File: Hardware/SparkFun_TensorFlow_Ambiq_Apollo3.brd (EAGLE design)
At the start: 40 x 40 mm, 95 parts, among them J5 CORTEX_DEBUG, J7 CAMERA-HIMAX, U2 LIS2DH12, U3 1.8V, U5 ARTEMIS_MODULESMD, Y2 32.768kHz

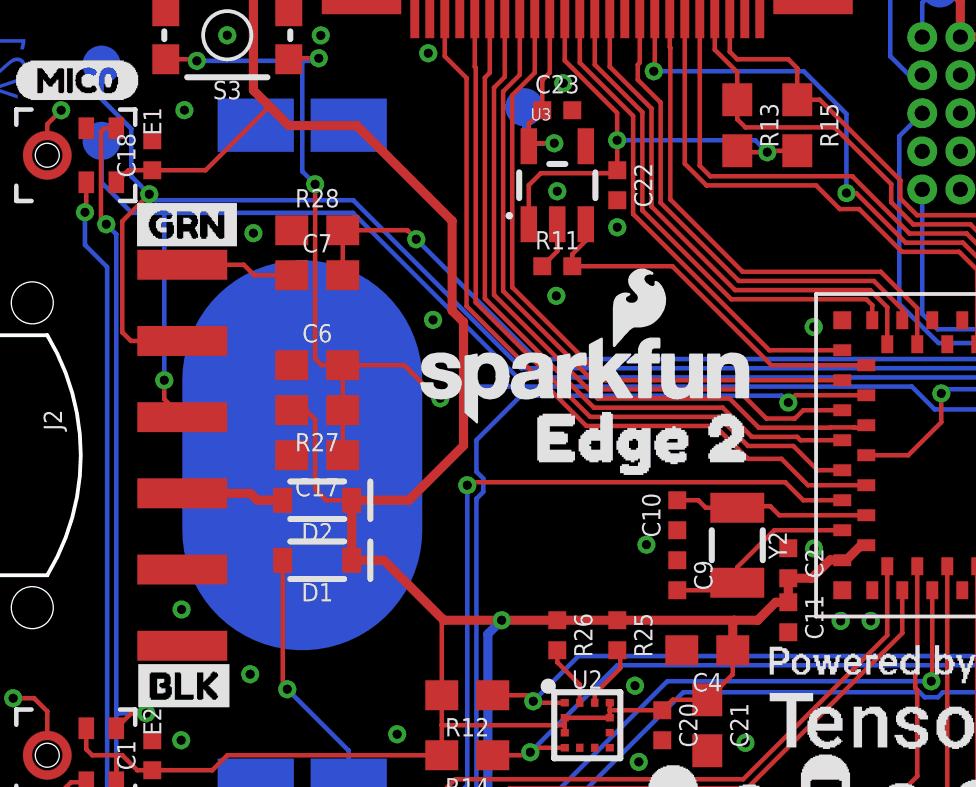
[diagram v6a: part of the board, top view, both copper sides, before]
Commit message: Move parts to fill gap left by DNP resistor removal. Change text in sch from Apollo3 to Artemis.
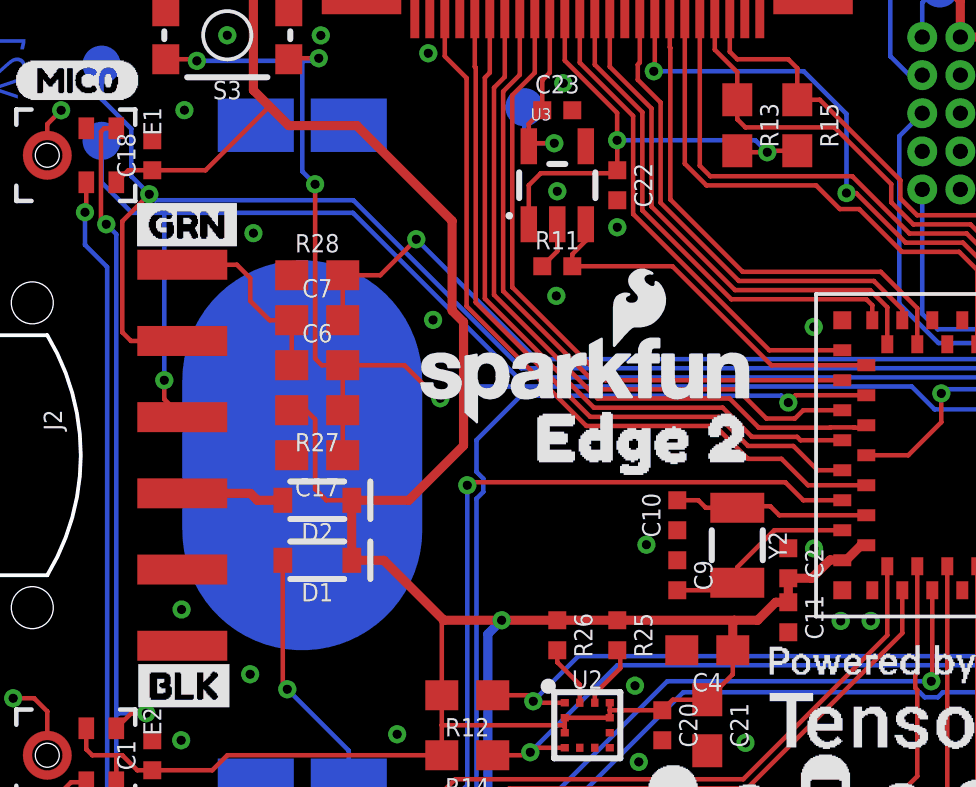
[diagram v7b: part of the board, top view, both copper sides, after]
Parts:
- moved C7 1.50 mm to (11.0, 24.5)
- moved R28 1.50 mm to (11.0, 26.0)
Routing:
- net !DTR: track 3.79 -> 6.36 mm
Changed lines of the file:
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@@
 <attribute name="VALUE" x="11" y="22.238" size="0.6096" layer="27" font="vector" ratio="20" align="top-center"/>
 </element>
-<element name="R28" library="SparkFun-Resistors" package="0603" value="220k" x="11" y="27.5" smashed="yes">
-<attribute name="NAME" x="11" y="28.262" size="0.6096" layer="25" font="vector" ratio="20" align="bottom-center"/>
-<attribute name="PROD_ID" value="RES-08969" x="11" y="23.69" size="1.778" layer="27" font="vector" ratio="15" display="off"/>
-<attribute name="VALUE" value="220k" x="11" y="26.738" size="0.6096" layer="27" font="vector" ratio="20" align="top-center"/>
-</element>
-<element name="C7" library="SparkFun-Capacitors" package="0603" value="0.1uF" x="11" y="26" smashed="yes">
+<element name="R28" library="SparkFun-Resistors" package="0603" value="220k" x="11" y="26" smashed="yes">
 <attribute name="NAME" x="11" y="26.762" size="0.6096" layer="25" font="vector" ratio="20" align="bottom-center"/>
-<attribute name="PROD_ID" value="CAP-00810" x="11" y="14.57" size="1.778" layer="27" font="vector" ratio="15" display="off"/>
-<attribute name="VALUE" value="0.1uF" x="11" y="25.238" size="0.6096" layer="27" font="vector" ratio="20" align="top-center"/>
+<attribute name="PROD_ID" value="RES-08969" x="11" y="22.19" size="1.778" layer="27" font="vector" ratio="15" display="off"/>
+<attribute name="VALUE" value="220k" x="11" y="25.238" size="0.6096" layer="27" font="vector" ratio="20" align="top-center"/>
+</element>
+<element name="C7" library="SparkFun-Capacitors" package="0603" value="0.1uF" x="11" y="24.5" smashed="yes">
+<attribute name="NAME" x="11" y="25.262" size="0.6096" layer="25" font="vector" ratio="20" align="bottom-center"/>
+<attribute name="PROD_ID" value="CAP-00810" x="11" y="13.07" size="1.778" layer="27" font="vector" ratio="15" display="off"/>
+<attribute name="VALUE" value="0.1uF" x="11" y="23.738" size="0.6096" layer="27" font="vector" ratio="20" align="top-center"/>
 </element>
 <element name="C17" library="SparkFun-Capacitors" package="0603" value="1nF" x="11" y="20" smashed="yes" rot="R180">
@@
 <wire x1="16.6858" y1="14.0408" x2="17.145" y2="14.5" width="0.3048" layer="16"/>
 <wire x1="26.7" y1="15.9" x2="26.7" y2="15.1" width="0.3048" layer="1"/>
-<wire x1="26.796" y1="15.1" x2="26.7" y2="15.1" width="0.3048" layer="1"/>
 <wire x1="24.9" y1="14.5" x2="25.68105" y2="14.5" width="0.3048" layer="1"/>
 <wire x1="26.28105" y1="15.1" x2="26.7" y2="15.1" width="0.3048" layer="1"/>
@@
 <contactref element="C7" pad="1"/>
 <contactref element="C6" pad="1"/>
-<wire x1="6.5" y1="26.35" x2="8.55" y2="26.35" width="0.1524" layer="1"/>
-<wire x1="8.55" y1="26.35" x2="8.9" y2="26" width="0.1524" layer="1"/>
-<wire x1="8.9" y1="26" x2="10.15" y2="26" width="0.1524" layer="1"/>
-<wire x1="10.15" y1="26" x2="10.15" y2="23" width="0" layer="19" extent="1-1"/>
+<wire x1="6.5" y1="26.35" x2="8.321" y2="26.35" width="0.1524" layer="1"/>
+<wire x1="8.321" y1="26.35" x2="8.763" y2="25.908" width="0.1524" layer="1"/>
+<wire x1="8.763" y1="25.908" x2="8.763" y2="25.146" width="0.1524" layer="1"/>
+<wire x1="8.763" y1="25.146" x2="9.409" y2="24.5" width="0.1524" layer="1"/>
+<wire x1="9.409" y1="24.5" x2="10.15" y2="24.5" width="0.1524" layer="1"/>
+<wire x1="10.15" y1="24.5" x2="10.15" y2="23" width="0.1524" layer="1"/>
 </signal>
 <signal name="V_BATT">
@@
 <contactref element="C7" pad="2"/>
 <contactref element="U5" pad="BOOT"/>
-<wire x1="11.85" y1="26" x2="11.85" y2="27.5" width="0.1524" layer="1"/>
+<wire x1="11.85" y1="24.5" x2="11.85" y2="26" width="0.1524" layer="1"/>
 <wire x1="36.5" y1="24.5" x2="36.5" y2="22.9" width="0.1524" layer="1"/>
 <via x="36.5" y="22.9" extent="1-16" drill="0.3048"/>
@@
 <via x="14.3" y="27.2" extent="1-16" drill="0.3048"/>
 <wire x1="35.05045625" y1="23.2048" x2="18.2952" y2="23.2048" width="0.1524" layer="16"/>
-<wire x1="11.85" y1="27.5" x2="14" y2="27.5" width="0.1524" layer="1"/>
-<wire x1="14" y1="27.5" x2="14.3" y2="27.2" width="0.1524" layer="1"/>
+<wire x1="14.3" y1="27.2" x2="13.1" y2="26" width="0.1524" layer="1"/>
+<wire x1="13.1" y1="26" x2="11.85" y2="26" width="0.1524" layer="1"/>
 </signal>
 <signal name="MIC_DATA">

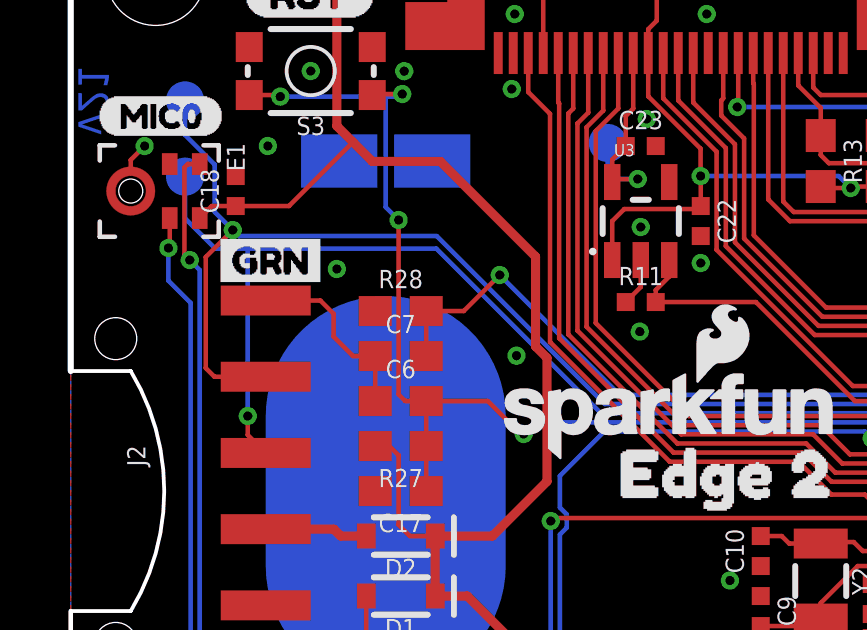
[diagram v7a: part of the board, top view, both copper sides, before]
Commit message: Add DNP resistor back to design to match production boards.
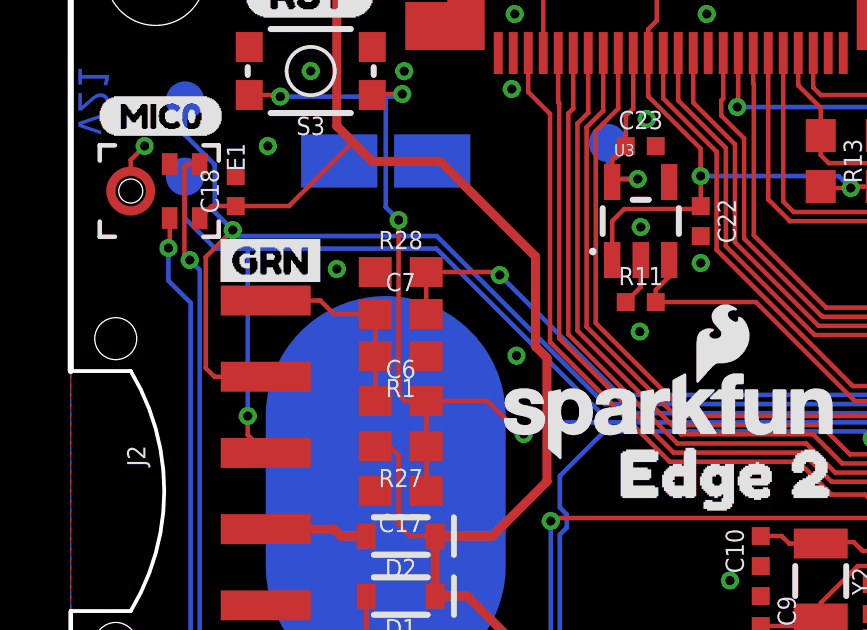
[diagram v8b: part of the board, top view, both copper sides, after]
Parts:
- added R1: DNP, SparkFun-Resistors:0603
- moved C7 1.40 mm to (11.0, 25.9)
- moved R28 1.30 mm to (11.0, 27.3)
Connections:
- net !DTR: now also R1.2
- net GND: now also R1.1
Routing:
- net BOOT: track 30.2 -> 29.7 mm
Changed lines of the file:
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@@
 <?xml version="1.0" encoding="utf-8"?>
 <!DOCTYPE eagle SYSTEM "eagle.dtd">
-<eagle version="9.4.2">
+<eagle version="9.5.0">
 <drawing>
 <settings>
@@
 <layer number="47" name="Measures" color="7" fill="1" visible="no" active="yes"/>
 <layer number="48" name="Document" color="7" fill="1" visible="no" active="yes"/>
-<layer number="49" name="Reference" color="7" fill="1" visible="no" active="yes"/>
+<layer number="49" name="Reference" color="7" fill="1" visible="yes" active="yes"/>
 <layer number="50" name="dxf" color="7" fill="1" visible="no" active="yes"/>
 <layer number="51" name="tDocu" color="6" fill="1" visible="yes" active="yes"/>
@@
 <attribute name="VALUE" x="11" y="22.238" size="0.6096" layer="27" font="vector" ratio="20" align="top-center"/>
 </element>
-<element name="R28" library="SparkFun-Resistors" package="0603" value="220k" x="11" y="26" smashed="yes">
-<attribute name="NAME" x="11" y="26.762" size="0.6096" layer="25" font="vector" ratio="20" align="bottom-center"/>
-<attribute name="PROD_ID" value="RES-08969" x="11" y="22.19" size="1.778" layer="27" font="vector" ratio="15" display="off"/>
-<attribute name="VALUE" value="220k" x="11" y="25.238" size="0.6096" layer="27" font="vector" ratio="20" align="top-center"/>
-</element>
-<element name="C7" library="SparkFun-Capacitors" package="0603" value="0.1uF" x="11" y="24.5" smashed="yes">
-<attribute name="NAME" x="11" y="25.262" size="0.6096" layer="25" font="vector" ratio="20" align="bottom-center"/>
-<attribute name="PROD_ID" value="CAP-00810" x="11" y="13.07" size="1.778" layer="27" font="vector" ratio="15" display="off"/>
-<attribute name="VALUE" value="0.1uF" x="11" y="23.738" size="0.6096" layer="27" font="vector" ratio="20" align="top-center"/>
+<element name="R28" library="SparkFun-Resistors" package="0603" value="220k" x="11" y="27.3" smashed="yes">
+<attribute name="NAME" x="11" y="28.062" size="0.6096" layer="25" font="vector" ratio="20" align="bottom-center"/>
+<attribute name="PROD_ID" value="RES-08969" x="11" y="23.49" size="1.778" layer="27" font="vector" ratio="15" display="off"/>
+<attribute name="VALUE" value="220k" x="11" y="26.538" size="0.6096" layer="27" font="vector" ratio="20" align="top-center"/>
+</element>
+<element name="C7" library="SparkFun-Capacitors" package="0603" value="0.1uF" x="11" y="25.9" smashed="yes">
+<attribute name="NAME" x="11" y="26.662" size="0.6096" layer="25" font="vector" ratio="20" align="bottom-center"/>
+<attribute name="PROD_ID" value="CAP-00810" x="11" y="14.47" size="1.778" layer="27" font="vector" ratio="15" display="off"/>
+<attribute name="VALUE" value="0.1uF" x="11" y="25.138" size="0.6096" layer="27" font="vector" ratio="20" align="top-center"/>
 </element>
 <element name="C17" library="SparkFun-Capacitors" package="0603" value="1nF" x="11" y="20" smashed="yes" rot="R180">
@@
 <attribute name="PROD_ID" value="CONN-14233" x="20" y="37" size="1.778" layer="27" font="vector" ratio="15" rot="R180" display="off"/>
 <attribute name="VALUE" x="20" y="37" size="0.6096" layer="27" font="vector" ratio="20" rot="R180" align="center"/>
+</element>
+<element name="R1" library="SparkFun-Resistors" package="0603" value="DNP" x="11" y="24.5" smashed="yes" rot="R180">
+<attribute name="NAME" x="11" y="23.738" size="0.6096" layer="25" font="vector" ratio="20" rot="R180" align="bottom-center"/>
+<attribute name="PROD_ID" value="RES-07828" x="11" y="24.5" size="1.778" layer="27" font="vector" ratio="15" rot="R180" display="off"/>
+<attribute name="VALUE" x="11" y="25.262" size="0.6096" layer="27" font="vector" ratio="20" rot="R180" align="top-center"/>
 </element>
 </elements>
@@
 <wire x1="2" y1="11.462" x2="1.562" y2="11.9" width="0.1524" layer="1"/>
 <via x="27.559" y="16.891" extent="1-16" drill="0.3048"/>
+<contactref element="R1" pad="1"/>
 </signal>
 <signal name="SWDCK">
@@
 <wire x1="6.5" y1="26.35" x2="8.321" y2="26.35" width="0.1524" layer="1"/>
 <wire x1="8.321" y1="26.35" x2="8.763" y2="25.908" width="0.1524" layer="1"/>
-<wire x1="8.763" y1="25.908" x2="8.763" y2="25.146" width="0.1524" layer="1"/>
-<wire x1="8.763" y1="25.146" x2="9.409" y2="24.5" width="0.1524" layer="1"/>
-<wire x1="9.409" y1="24.5" x2="10.15" y2="24.5" width="0.1524" layer="1"/>
+<wire x1="8.763" y1="25.908" x2="8.763" y2="25.9" width="0.1524" layer="1"/>
+<contactref element="R1" pad="2"/>
+<wire x1="10.15" y1="25.9" x2="10.15" y2="24.5" width="0.1524" layer="1"/>
 <wire x1="10.15" y1="24.5" x2="10.15" y2="23" width="0.1524" layer="1"/>
+<wire x1="8.763" y1="25.9" x2="10.15" y2="25.9" width="0.1524" layer="1"/>
 </signal>
 <signal name="V_BATT">
@@
 <contactref element="C7" pad="2"/>
 <contactref element="U5" pad="BOOT"/>
-<wire x1="11.85" y1="24.5" x2="11.85" y2="26" width="0.1524" layer="1"/>
+<wire x1="11.85" y1="25.9" x2="11.85" y2="27.3" width="0.1524" layer="1"/>
 <wire x1="36.5" y1="24.5" x2="36.5" y2="22.9" width="0.1524" layer="1"/>
 <via x="36.5" y="22.9" extent="1-16" drill="0.3048"/>
@@
 <via x="14.3" y="27.2" extent="1-16" drill="0.3048"/>
 <wire x1="35.05045625" y1="23.2048" x2="18.2952" y2="23.2048" width="0.1524" layer="16"/>
-<wire x1="14.3" y1="27.2" x2="13.1" y2="26" width="0.1524" layer="1"/>
-<wire x1="13.1" y1="26" x2="11.85" y2="26" width="0.1524" layer="1"/>
+<wire x1="14.3" y1="27.2" x2="14.2" y2="27.3" width="0.1524" layer="1"/>
+<wire x1="14.2" y1="27.3" x2="11.85" y2="27.3" width="0.1524" layer="1"/>
 </signal>
 <signal name="MIC_DATA">
